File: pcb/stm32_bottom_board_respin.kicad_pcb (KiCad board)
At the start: 2 copper layers, 90 x 60 mm, 69 parts, among them J1 Conn_01x02, J10 Conn_01x08, J11 Conn_01x04, J12 Conn_01x04, J2 WS2812, J3 FAN_PWM, J4 SSR, J5 PURFUME, J6 Conn_01x14, J7 Conn_01x12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

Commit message: update,
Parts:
- removed REF** (x4): MountingHole_3.2mm_M3_DIN965, MountingHole:MountingHole_3.2mm_M3_DIN965
- moved C15 42.4 mm to (39.0, 83.0)
- moved D3 42.4 mm to (39.6, 43.2)
- moved D5 42.4 mm to (64.3, 83.8)
- moved J8 42.4 mm to (62.6, 79.0)
- moved Q3 42.4 mm to (97.3, 70.1)
- moved R10 42.4 mm to (79.2, 73.6)
- moved R2 42.4 mm to (76.1, 87.2)
- moved R5 42.4 mm to (87.9, 74.3)
- moved R6 42.4 mm to (99.3, 77.5)
- moved SW1 42.4 mm to (45.8, 75.2)
- moved C1 42.4 mm to (98.7, 53.4)
- moved C11 42.4 mm to (51.0, 71.4)
- moved C12 42.4 mm to (51.0, 67.2)
- moved C13 42.4 mm to (54.6, 58.0)
- moved C14 42.4 mm to (56.3, 56.0)
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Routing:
- net GND: track 582.8 -> 599.9 mm
- net +3V3: track 249.4 -> 257.4 mm
- net /FAN_PWM_OUTPUT: track 39.2 -> 34.7 mm
- net /STM32_CORE/SWIO: track 35.2 -> 37.8 mm
- net /STM32_CORE/SWCLK: track 26.6 -> 28.4 mm
- net +5V: track 292.0 -> 293.6 mm
- net Net-(D3-Pad1): track 3.05 -> 4.11 mm
- net Net-(D2-Pad1): track 3.81 -> 4.50 mm
- removed copper zone on B.Cu, net GND
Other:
- board size 90 x 60 mm -> 100 x 70 mm

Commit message: update,
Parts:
- J9: value SSR -> IONAIR_COMM
- SW1: footprint Button_Switch_SMD:SW_SPST_CK_RS282G05A3 -> Button_Switch_SMD:SW_SPST_PTS645
- moved SW1 4.71 mm to (42.1, 72.3)
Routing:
- net /STM32_CORE/RESET: track 38.4 -> 51.6 mm
- net GND: track 599.9 -> 597.6 mm

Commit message: add .gitignore .gitattributes,
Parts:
- J9: value IONAIR_COMM -> SSR
- Y2: value O32.768K -> O_EPSON_32.768K; footprint Crystal:Crystal_SMD_MicroCrystal_CC7V-T1A-2Pin_3.2x1.5mm_HandSoldering -> footprint-lib:MC-306
- moved C14 4.28 mm to (54.8, 52.0), turned to 180 degrees
- moved Y2 4.17 mm to (54.8, 55.0), turned to 180 degrees
- moved C13 0.11 mm to (54.7, 58.0), turned to 180 degrees
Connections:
- Y2 pad 1: /STM32_CORE/PC15 -> /STM32_CORE/PC14
- Y2 pad 2: /STM32_CORE/PC14 -> (no net)
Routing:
- net GND: track 597.6 -> 612.8 mm
- net +3V3: track 257.4 -> 261.2 mm
- net +5V: track 293.6 -> 289.8 mm
- net /STM32_CORE/PC14: track 11.8 -> 14.9 mm
- net /STM32_CORE/RESET: track 51.6 -> 53.9 mm
- net /STM32_CORE/PC15: track 12.8 -> 13.3 mm

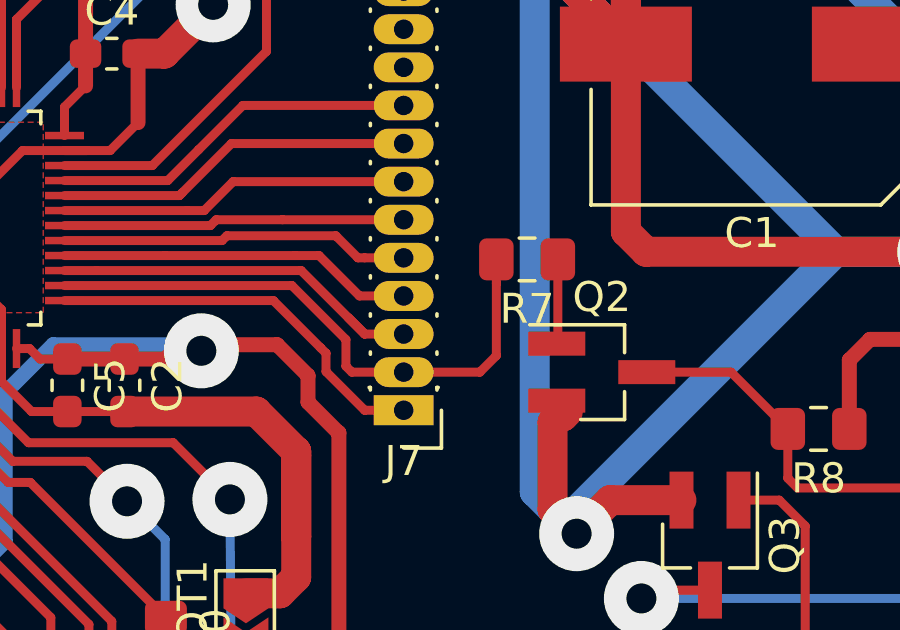
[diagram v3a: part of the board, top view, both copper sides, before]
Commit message: update FAN PWM to PA8
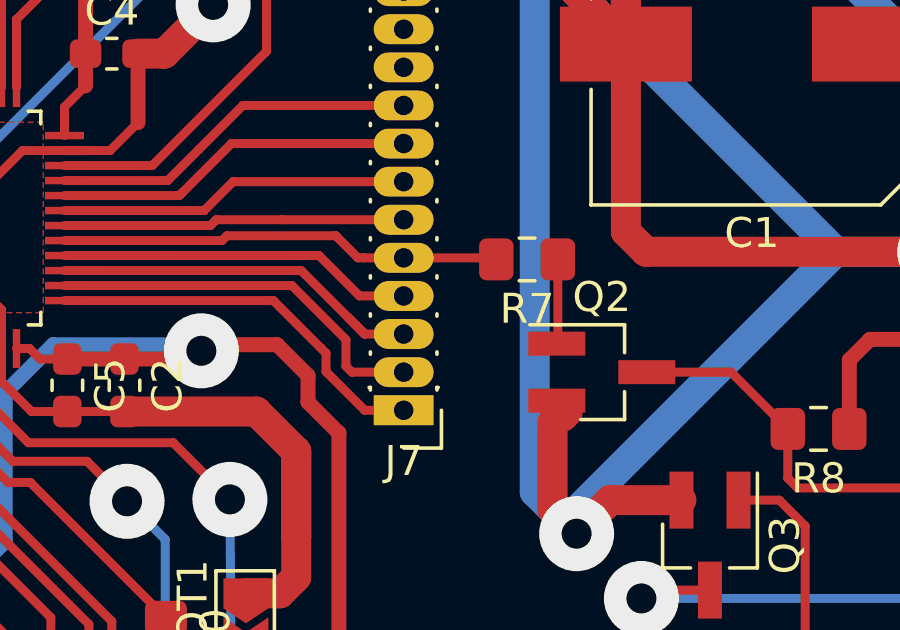
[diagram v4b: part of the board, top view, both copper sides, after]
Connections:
- J7 pad 2: STM32_FAN_PWM_OUTPUT -> /STM32_CORE/PB13
- J7 pad 5: /STM32_CORE/PA8 -> STM32_FAN_PWM_OUTPUT
- U3 pad 26: STM32_FAN_PWM_OUTPUT -> /STM32_CORE/PB13
- U3 pad 29: /STM32_CORE/PA8 -> STM32_FAN_PWM_OUTPUT
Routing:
- net /STM32_CORE/PB13: track 0.00 -> 13.0 mm
- net /STM32_CORE/PA8: track 11.7 -> 0.00 mm
- net STM32_FAN_PWM_OUTPUT: track 19.5 -> 14.8 mm

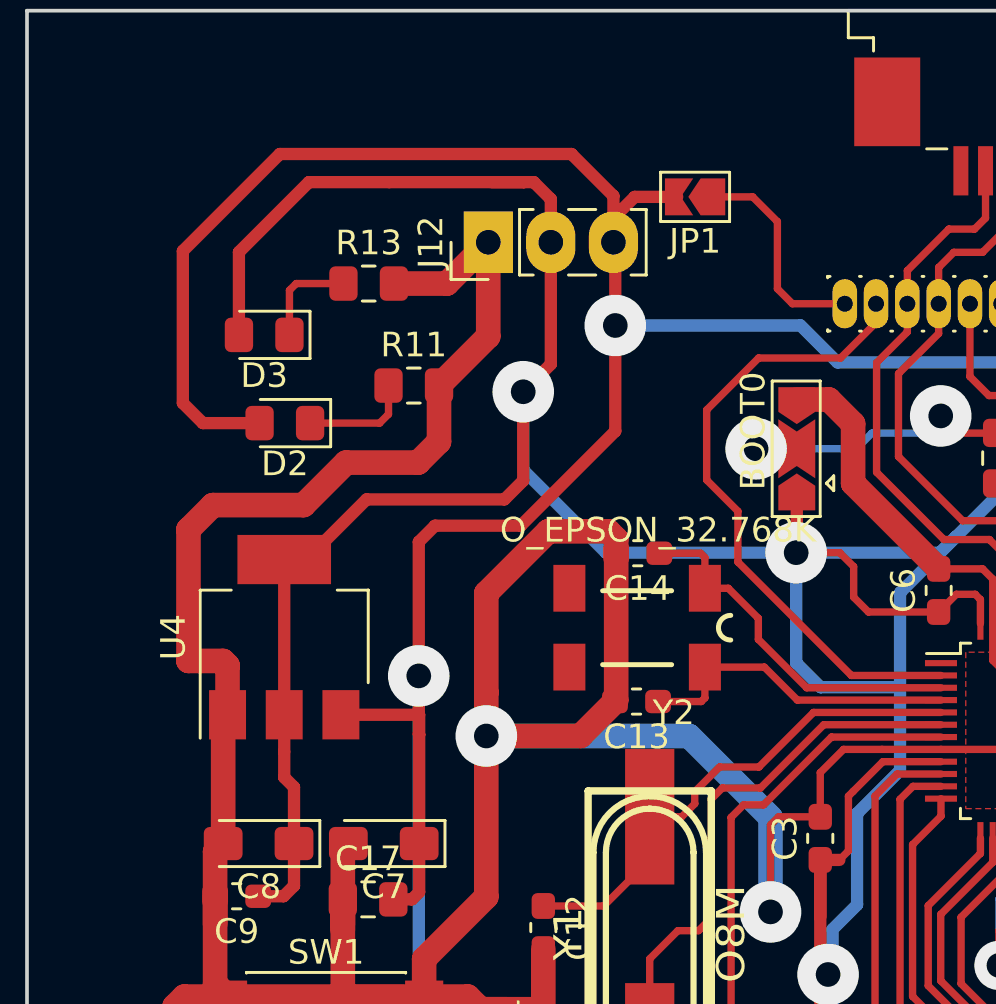
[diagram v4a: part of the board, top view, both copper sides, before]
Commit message: add capacitor to the main 5V
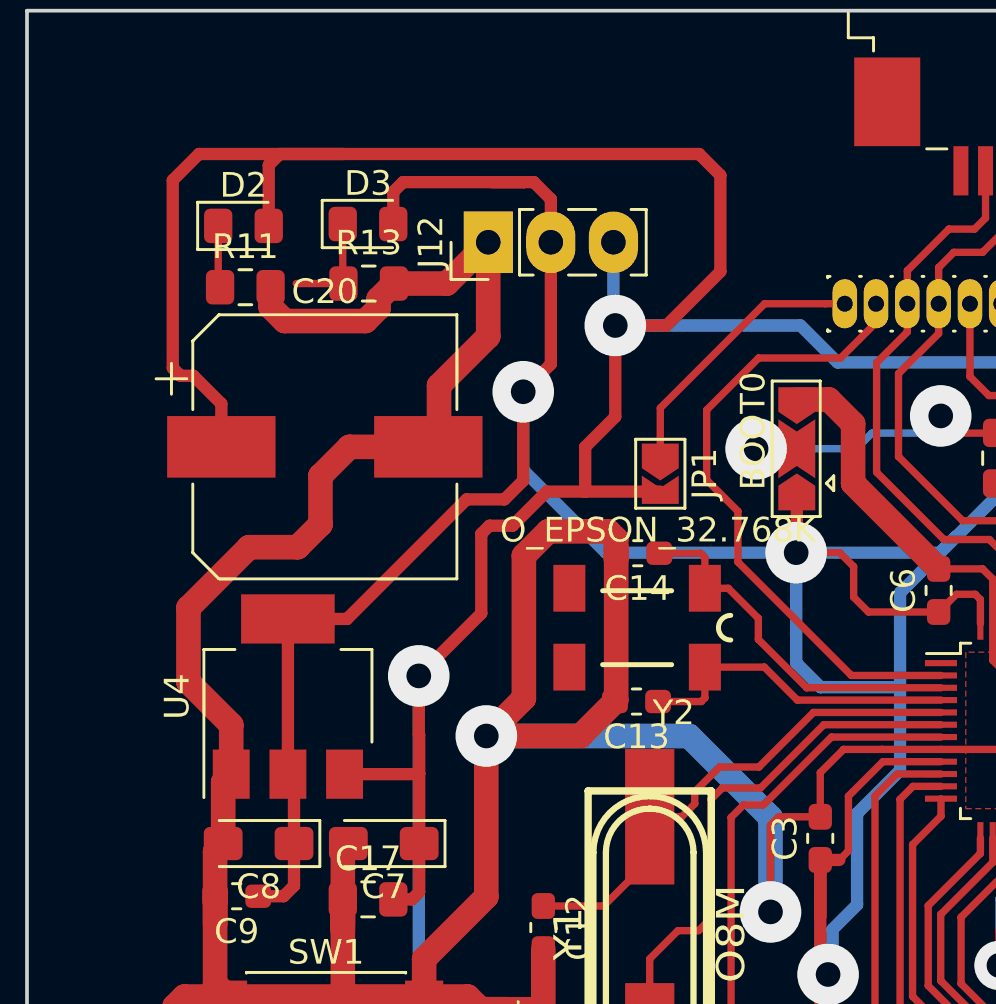
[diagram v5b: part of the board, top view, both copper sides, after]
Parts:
- added C20: CP220uf,50V, Capacitor_SMD:CP_Elec_10x10.5, F.Cu at (42.1, 47.7)
- moved JP1 11.3 mm to (55.7, 48.8), turned to 270 degrees
- moved D2 8.18 mm to (38.8, 38.7), turned to 0 degrees
- moved R11 7.91 mm to (38.9, 41.2)
- moved D3 6.16 mm to (43.8, 38.7), turned to 0 degrees
- moved U4 2.42 mm to (40.6, 57.8)
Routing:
- net +5V: track 289.8 -> 305.9 mm
- net +3V3: track 261.2 -> 250.2 mm
- net GND: track 612.8 -> 617.8 mm
- net Net-(D2-Pad1): track 4.50 -> 2.52 mm
- net Net-(J6-Pad14): track 9.22 -> 11.2 mm

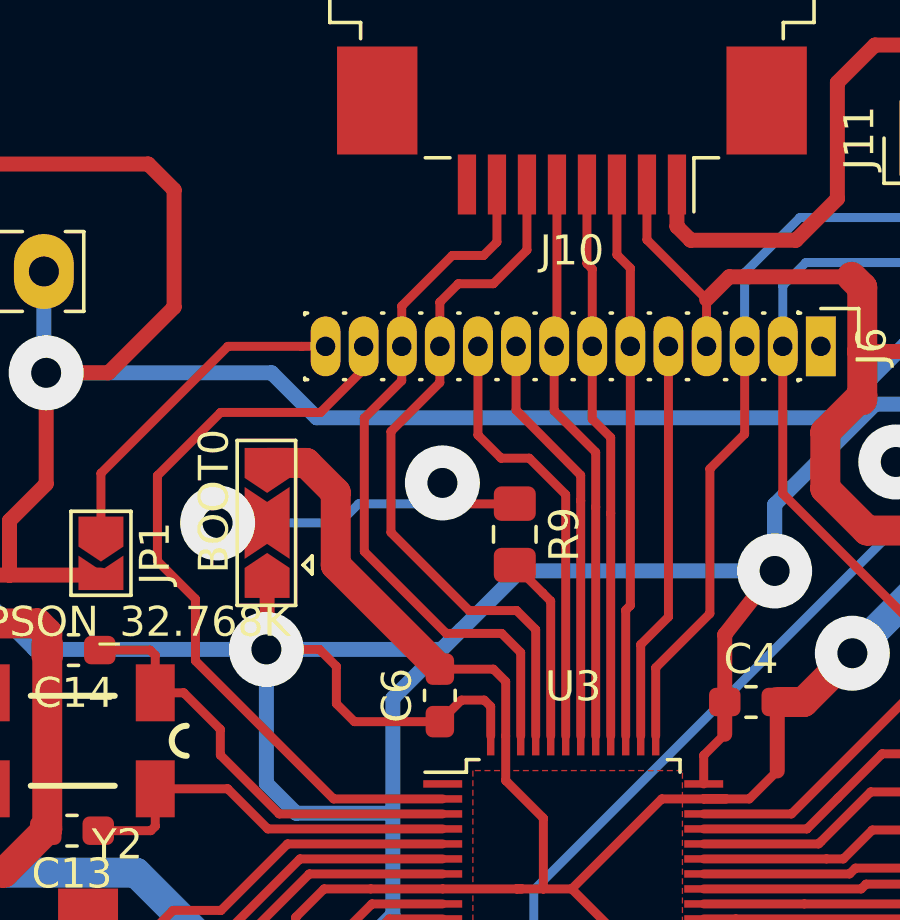
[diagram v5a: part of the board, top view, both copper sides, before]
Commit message: fix I2C pin on PCB,
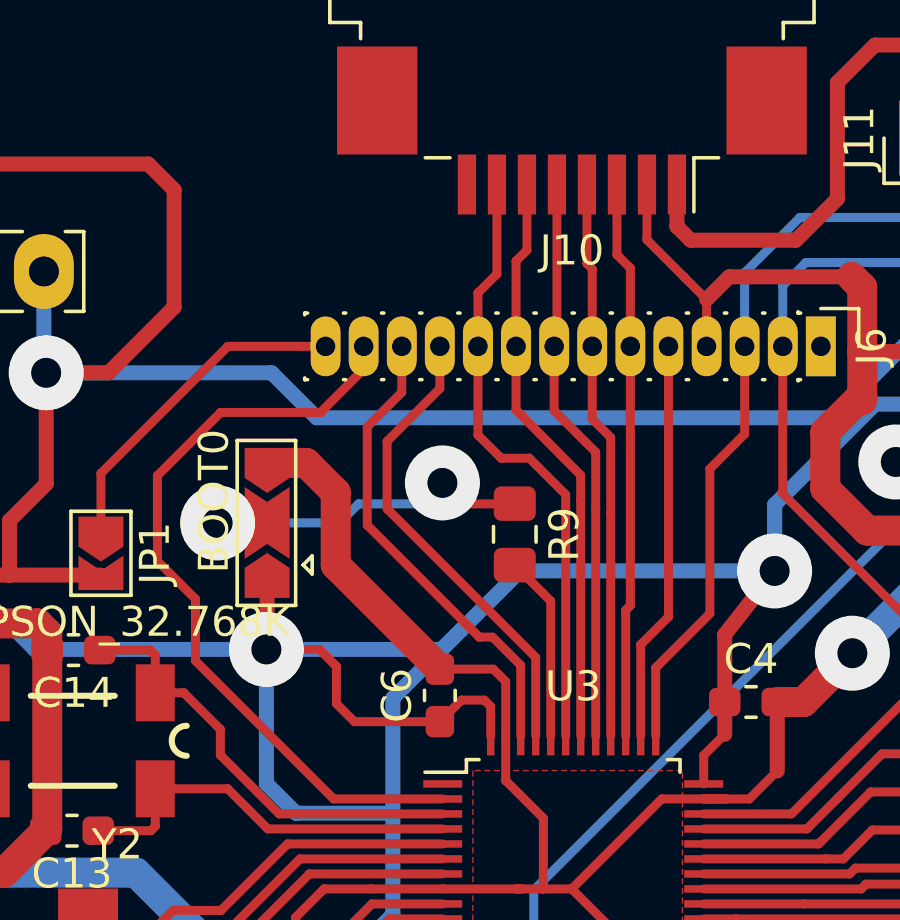
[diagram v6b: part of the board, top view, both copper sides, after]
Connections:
- net /STM32_CORE/PA10 renamed PMS5003S_RX
- net /STM32_CORE/PA9 renamed PMS5003S_TX
- J6 pad 10: /STM32_CORE/PB7 -> I2C_SDA
- J6 pad 11: I2C_SCL -> /STM32_CORE/PB8
- J6 pad 12: I2C_SDA -> /STM32_CORE/PB9
- J6 pad 9: /STM32_CORE/PB6 -> I2C_SCL
- U3 pad 42: /STM32_CORE/PB6 -> I2C_SCL
- U3 pad 43: /STM32_CORE/PB7 -> I2C_SDA
- U3 pad 45: I2C_SCL -> /STM32_CORE/PB8
- U3 pad 46: I2C_SDA -> /STM32_CORE/PB9
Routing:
- net /STM32_CORE/PB9: track 0.00 -> 15.8 mm
- net /STM32_CORE/PB8: track 0.00 -> 15.8 mm
- net /STM32_CORE/PB7: track 14.7 -> 0.00 mm
- net /STM32_CORE/PB6: track 13.9 -> 0.00 mm
- net I2C_SCL: track 23.9 -> 19.4 mm
- net I2C_SDA: track 24.1 -> 20.4 mm

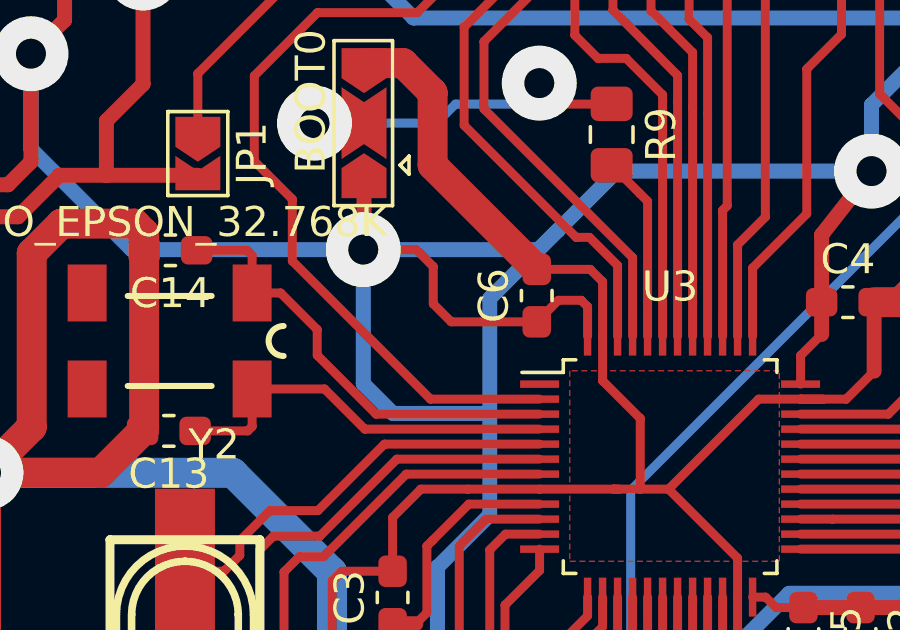
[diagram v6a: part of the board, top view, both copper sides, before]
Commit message: update VBAT pin with 3V3,
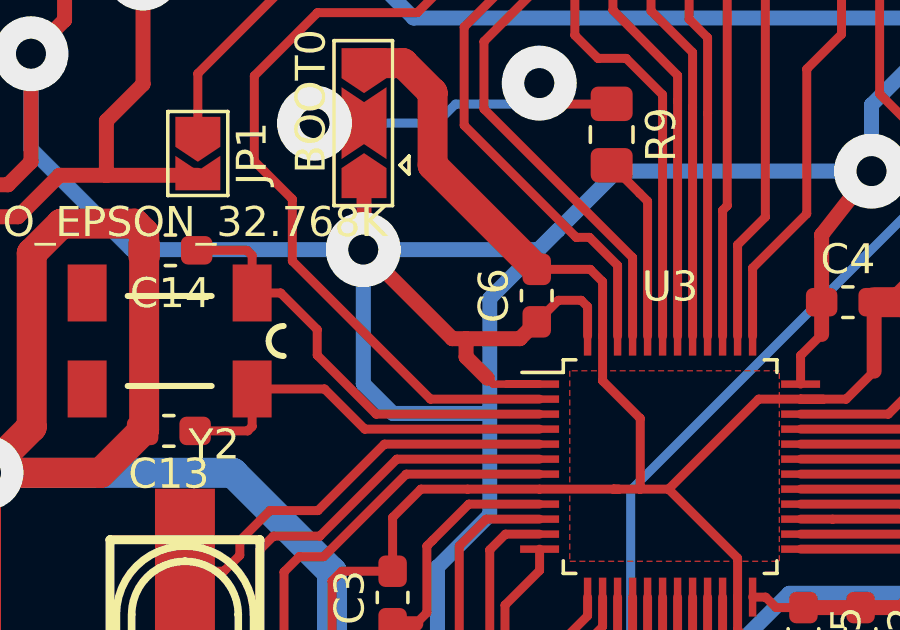
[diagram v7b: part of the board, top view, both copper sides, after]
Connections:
- U3 pad 1: /STM32_CORE/VBAT -> +3V3
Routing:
- net +3V3: track 250.2 -> 254.5 mm

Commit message: update,
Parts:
- added J13: Conn_01x03, footprint-lib:mpt_0,5%2f3-2,54, F.Cu at (94.9, 55.6)
- moved C1 5.84 mm to (104.5, 53.4)
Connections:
- net PMS5003S_RX renamed STM32_PMS5003S_RX
- net PMS5003S_TX renamed STM32_PMS5003S_TX
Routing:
- net GND: track 617.8 -> 606.2 mm
- net STM32_PMS5003S_RX: track 11.7 -> 21.6 mm
- net STM32_PMS5003S_TX: track 11.4 -> 20.7 mm
